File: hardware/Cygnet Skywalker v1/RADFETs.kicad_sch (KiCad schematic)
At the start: 14 parts, among them Q1 NJFET, Q2 NJFET, Q5 NJFET, Q6 NMOS, Q7 NMOS, Q8 NJFET, U10 INA260, U11 RM-VT01-A Readout Module, U12 VT01, U4 INA260, U6 VT01

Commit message: minor progress on pcb design
- more decoupling caps
- i2c address config
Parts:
- added C20, C21: 100n, symbol Device:C
- added C26: 10u, symbol Device:C
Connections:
- net +12V: now also C26.1
- net +3.3V: now also C20.1, C21.1
- net GND: now also C20.2, C21.2, C26.2

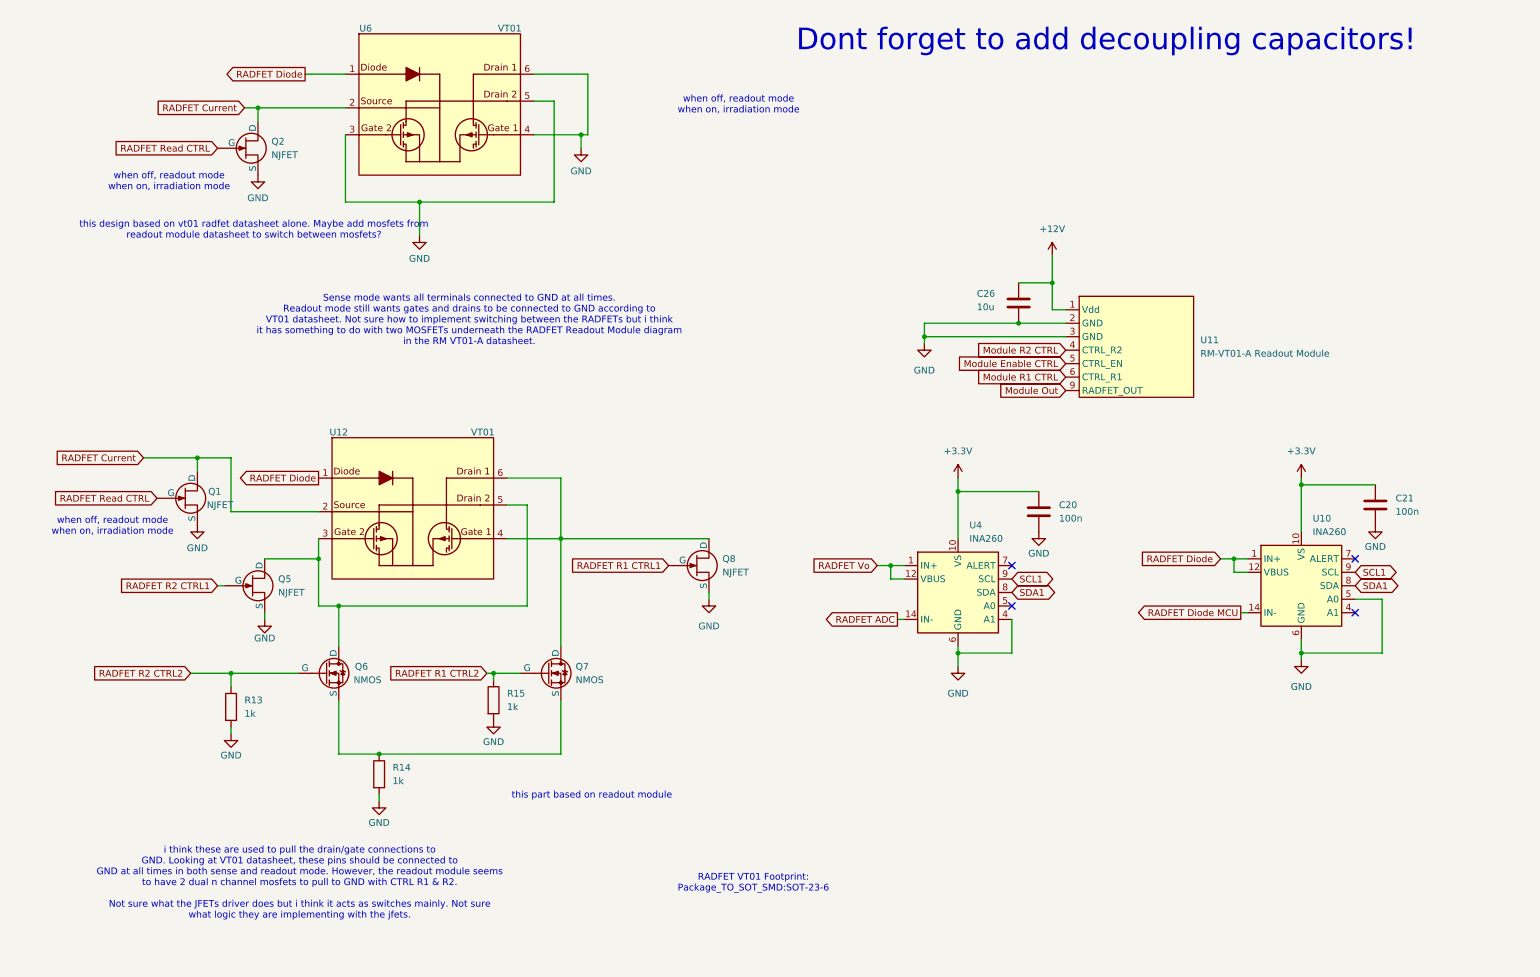
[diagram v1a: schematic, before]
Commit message: updated progress on PCB
-implemented 3.3v to 12v boost converter
-radfet readout circuitry done (i think)
-added readout circuitry from oresat & proves fc v5c board
-finished gps schematic (need footprint still)
-added few LEDs

main priorities:
-watchdog circuit
-calculate voltage div resistor values for 12v
-gps footprint
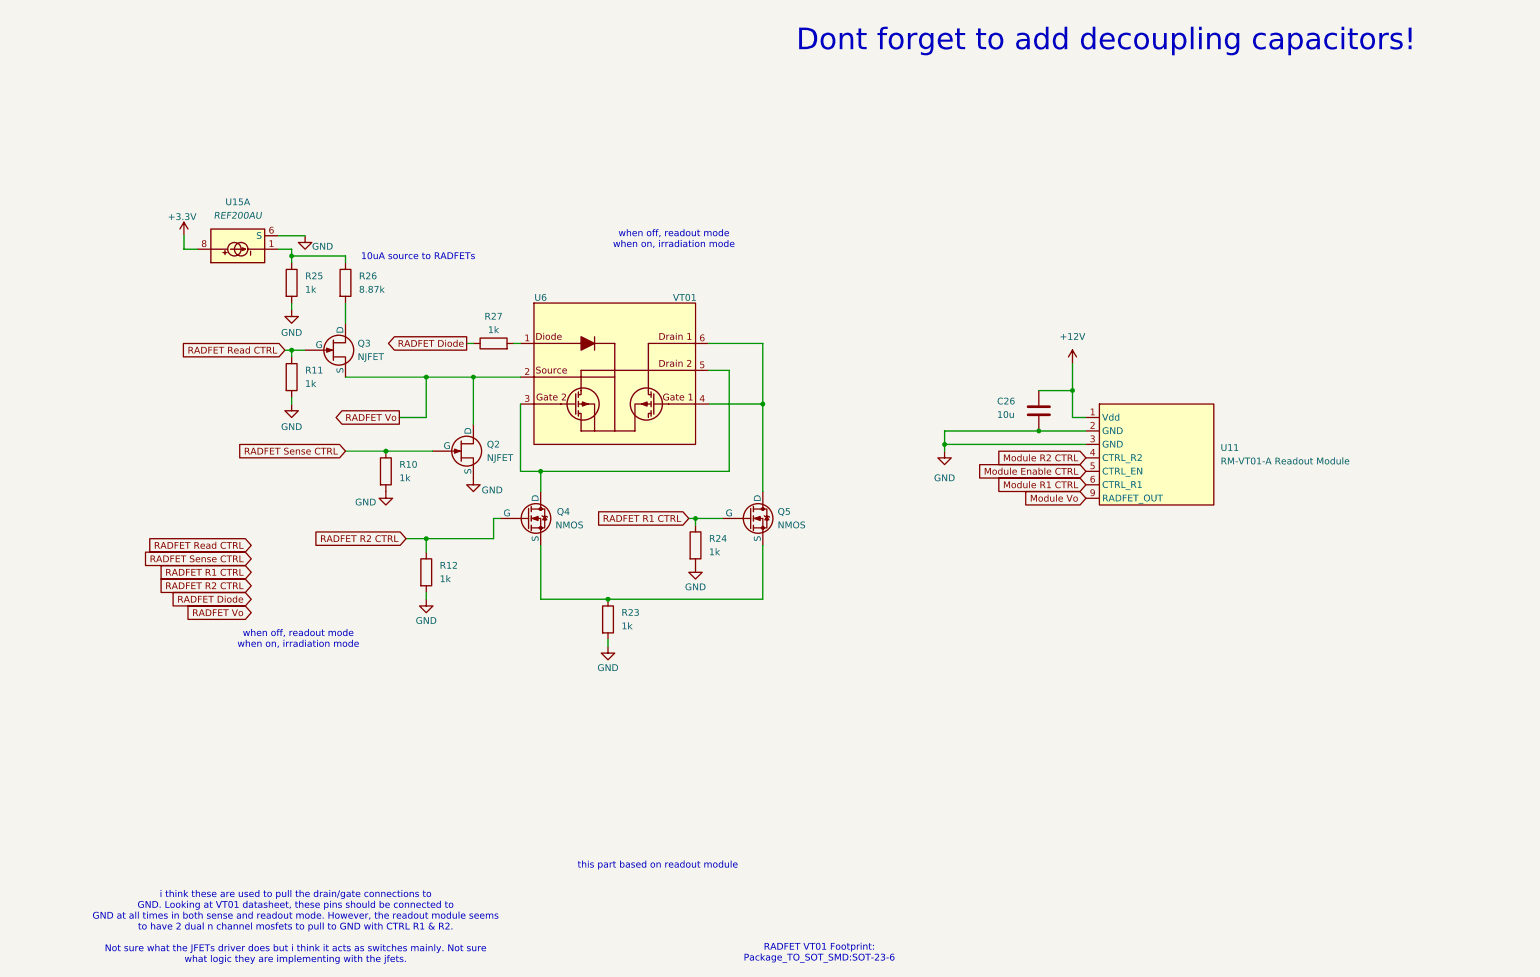
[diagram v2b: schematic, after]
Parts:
- removed C20, C21: 100n, symbol Device:C
- removed Q1, Q5, Q8: NJFET, symbol Simulation_SPICE:NJFET
- removed Q6, Q7: NMOS, symbol Simulation_SPICE:NMOS
- removed R13, R14, R15: 1k, symbol Device:R
- removed U10, U4: INA260, Package_SO:TSSOP-16_4.4x5mm_P0.65mm, symbol Sensor:INA260
- removed U12: VT01, Package_TO_SOT_SMD:SOT-23-6, symbol Varadis_RADFETs:VT01
- added Q3: NJFET, symbol Simulation_SPICE:NJFET
- added Q4, Q5: NMOS, symbol Simulation_SPICE:NMOS
- added R10, R11, R12, R23, R24, R25, R27: 1k, symbol Device:R
- added R26: 8.87k, symbol Device:R
- added U15: REF200AU, Package_SO:SOIC-8_3.9x4.9mm_P1.27mm, symbol Reference_Current:REF200AU
- U11: footprint (none) -> Skywalkerfeet:RM-VT01-A
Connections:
- net RADFET Current is gone; now on net RADFET Vo: Q2.1 (D), U6.2
- net +3.3V: now also U15.8
- net GND: now also R10.2, R11.2, R12.2, R23.2, R24.2, R25.2, U15.6 (S); no longer U6.3, U6.4, U6.5, U6.6
- net RADFET Diode: now also R27.1; no longer U6.1
- net RADFET Read CTRL: now also Q3.2 (G), R11.1; no longer Q2.2 (G)
- net RADFET Vo: now also Q3.3 (S)
- net Module Out renamed Module Vo
- new net: R27.2, U6.1
- new net: Q4.1 (D), U6.3, U6.5
- new net: Q5.1 (D), U6.4, U6.6
- new net: Q4.3 (S), Q5.3 (S), R23.1
- new net: Q3.1 (D), R26.2
- new net: R25.1, R26.1, U15.1
- new net RADFET R1 CTRL: Q5.2 (G), R24.1
- new net RADFET R2 CTRL: Q4.2 (G), R12.1
- new net RADFET Sense CTRL: Q2.2 (G), R10.1
- no-connect marks 4 -> 0
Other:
- note added: "10uA source to RADFETs"
- note removed: "Sense mode wants all terminals connected to GND at all times. Readout mode still wants gates and drains to be connected to GND according to VT01 datasheet. Not sure how to implement switching between the RADFETs but i think it has something to do with two MOSFETs underneath the RADFET Readout Module diagram in the RM VT01-A datasheet."
- note removed: "this design based on vt01 radfet datasheet alone. Maybe add mosfets from readout module datasheet to switch between mosfets?"
- moved on the sheet: C26, Q2, U11, U6

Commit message: carried over changes to schematic made on max's branch
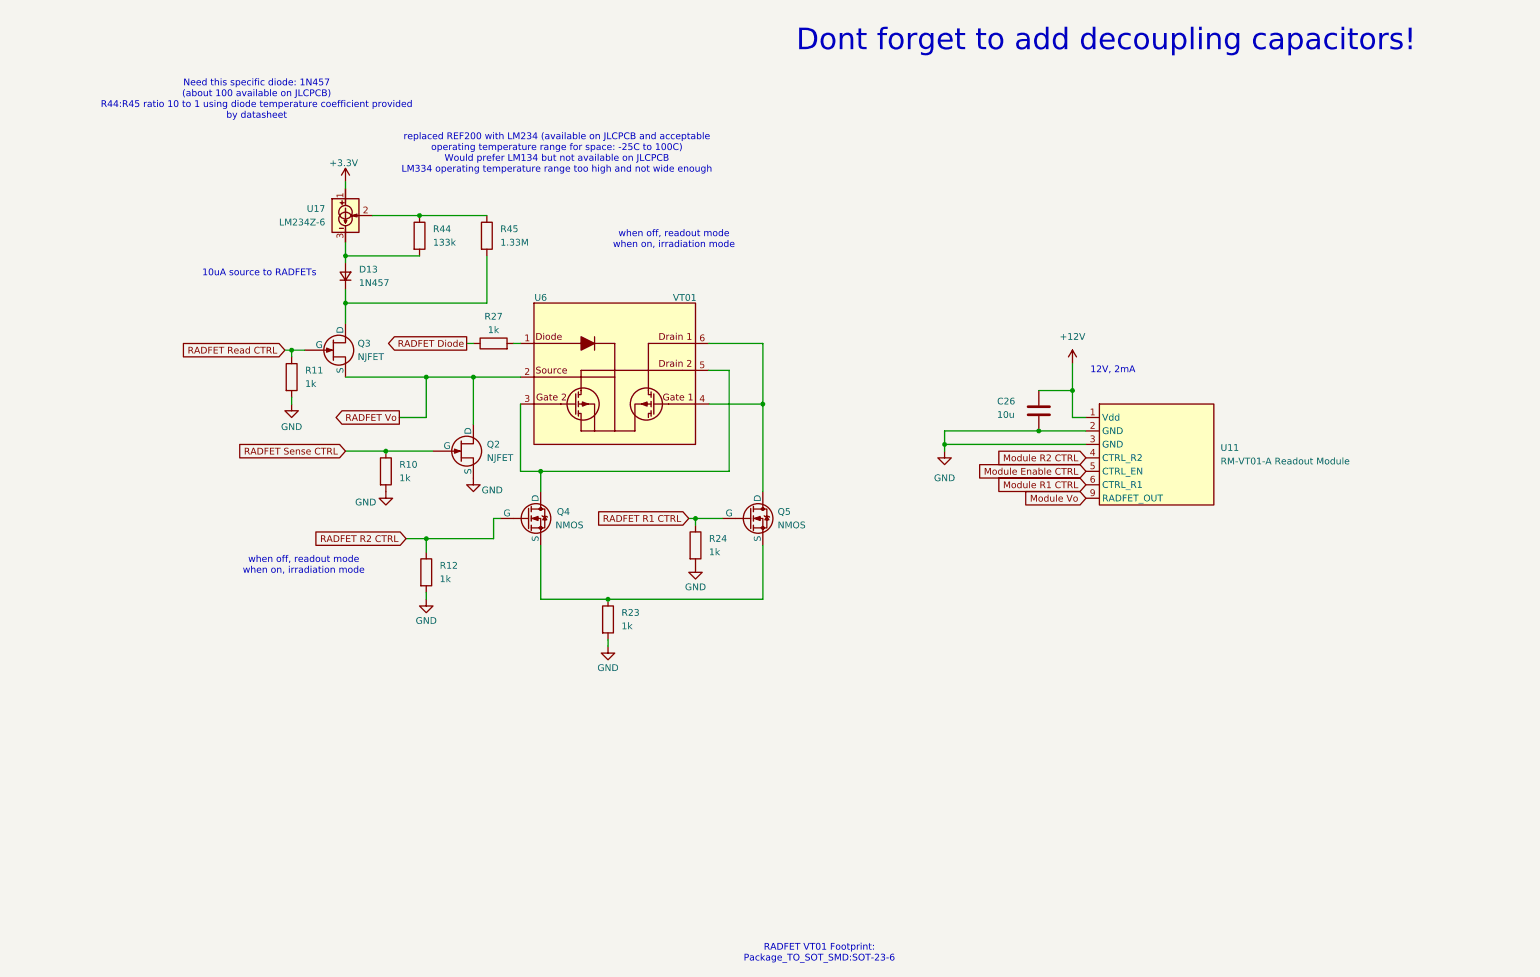
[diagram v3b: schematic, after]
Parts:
- removed R25: 1k, symbol Device:R
- removed R26: 8.87k, symbol Device:R
- removed U15: REF200AU, Package_SO:SOIC-8_3.9x4.9mm_P1.27mm, symbol Reference_Current:REF200AU
- added D13: 1N457, symbol Device:D_Small
- added R44: 133k, symbol Device:R
- added R45: 1.33M, symbol Device:R
- added U17: LM234Z-6, Package_TO_SOT_THT:TO-92_Inline, symbol Reference_Current:LM234Z-6
- C26: footprint (none) -> Capacitor_SMD:C_0402_1005Metric
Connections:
- net +3.3V: now also U17.1
- net at Q3.1 (D): now also D13.1 (K), R45.2
- new net: R44.1, R45.1, U17.2
- new net: D13.2 (A), R44.2, U17.3
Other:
- note added: "12V, 2mA"
- note added: "Need this specific diode: 1N457 (about 100 available on JLCPCB) R44:R45 ratio 10 to 1 using diode temperature coefficient provided by datasheet"
- note added: "replaced REF200 with LM234 (available on JLCPCB and acceptable operating temperature range for space: -25C to 100C) Would prefer LM134 but not available on JLCPCB LM334 operating temperature range too high and not wide enough"
- note removed: "i think these are used to pull the drain/gate connections to GND. Looking at VT01 datasheet, these pins should be connected to GND at all times in both sense and readout mode. However, the readout module seems to have 2 dual n channel mosfets to pull to GND with CTRL R1 & R2. Not sure what the JFETs driver does but i think it acts as switches mainly. Not sure what logic they are implementing with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"
- note removed: "this part based on readout module"

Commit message: brought over changes made on max branch
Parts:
- added C32: 10u, Capacitor_SMD:C_0402_1005Metric, symbol Device:C
- renumbered C26 to C33, D13 to D11, R44 to R21, R45 to R22, R27 to R23, R11 to R24, R10 to R25, R12 to R26, R24 to R27, R23 to R28
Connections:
- net +3.3V: now also C32.1
- net GND: now also C32.2
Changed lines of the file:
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@@
+	)
+	(junction
+		(at 68.58 41.91)
+		(diameter 0)
+		(color 0 0 0 0)
 	)
 	(junction
@@
 	(wire
 		(pts
+			(xy 68.58 41.91) (xy 68.58 49.53)
+		)
+		(stroke
+			(width 0)
+			(type default)
+		)
+	)
+	(wire
+		(pts
 			(xy 96.52 115.57) (xy 96.52 111.76)
 		)
@@
 	(wire
 		(pts
-			(xy 68.58 48.26) (xy 68.58 49.53)
+			(xy 68.58 40.64) (xy 68.58 41.91)
 		)
 		(stroke
@@
 		(pts
 			(xy 147.32 90.17) (xy 147.32 78.74)
+		)
+		(stroke
+			(width 0)
+			(type default)
+		)
+	)
+	(wire
+		(pts
+			(xy 57.15 41.91) (xy 68.58 41.91)
 		)
 		(stroke
@@
 		(dnp no)
 		(fields_autoplaced yes)
-		(property "Reference" "R23"
+		(property "Reference" "R28"
 			(at 120.65 129.5399 0)
 			(effects
@@
 			(project "Cygnet Skywalker v1"
 				(path "/f674abc6-f811-4b69-a04b-9059ca6b6a44/33e54b08-8438-48ba-af26-405155868428"
-					(reference "R23")
+					(reference "R28")
 					(unit 1)
 				)
@@
 		(dnp no)
 		(fields_autoplaced yes)
-		(property "Reference" "R12"
+		(property "Reference" "R26"
 			(at 86.36 120.6499 0)
 			(effects
@@
 			(project "Cygnet Skywalker v1"
 				(path "/f674abc6-f811-4b69-a04b-9059ca6b6a44/33e54b08-8438-48ba-af26-405155868428"
-					(reference "R12")
+					(reference "R26")
 					(unit 1)
 				)
@@
 		(on_board yes)
 		(dnp no)
-		(property "Reference" "C26"
+		(property "Reference" "C33"
 			(at 191.516 89.662 0)
 			(effects
@@
 			(project "Cygnet Skywalker v1"
 				(path "/f674abc6-f811-4b69-a04b-9059ca6b6a44/33e54b08-8438-48ba-af26-405155868428"
-					(reference "C26")
+					(reference "C33")
 					(unit 1)
 				)
@@
 		(dnp no)
 		(fields_autoplaced yes)
-		(property "Reference" "R11"
+		(property "Reference" "R24"
 			(at 60.96 83.8199 0)
 			(effects
@@
 			(project "Cygnet Skywalker v1"
 				(path "/f674abc6-f811-4b69-a04b-9059ca6b6a44/33e54b08-8438-48ba-af26-405155868428"
-					(reference "R11")
+					(reference "R24")
 					(unit 1)
 				)
@@
 		(on_board yes)
 		(dnp no)
-		(property "Reference" "R27"
+		(property "Reference" "R23"
 			(at 96.52 73.66 90)
 			(effects
@@
 			(project "Cygnet Skywalker v1"
 				(path "/f674abc6-f811-4b69-a04b-9059ca6b6a44/33e54b08-8438-48ba-af26-405155868428"
-					(reference "R27")
+					(reference "R23")
 					(unit 1)
 				)
@@
 	(symbol
 		(lib_id "power:+3.3V")
-		(at 68.58 48.26 0)
+		(at 68.58 40.64 0)
 		(unit 1)
 		(exclude_from_sim no)
@@
 		(dnp no)
 		(property "Reference" "#PWR0105"
-			(at 68.58 52.07 0)
+			(at 68.58 44.45 0)
 			(effects
 				(font
@@
 		)
 		(property "Value" "+3.3V"
-			(at 65.532 44.704 0)
+			(at 65.532 37.084 0)
 			(effects
 				(font
@@
 		)
 		(property "Footprint" ""
-			(at 68.58 48.26 0)
+			(at 68.58 40.64 0)
 			(effects
 				(font
@@
 		)
 		(property "Datasheet" ""
-			(at 68.58 48.26 0)
+			(at 68.58 40.64 0)
 			(effects
 				(font
@@
 		)
 		(property "Description" "Power symbol creates a global label with name \"+3.3V\""
-			(at 68.58 48.26 0)
+			(at 68.58 40.64 0)
 			(effects
 				(font
@@
 		(dnp no)
 		(fields_autoplaced yes)
-		(property "Reference" "R45"
+		(property "Reference" "R22"
 			(at 97.79 57.1499 0)
 			(effects
@@
 			(project "Cygnet Skywalker v1"
 				(path "/f674abc6-f811-4b69-a04b-9059ca6b6a44/33e54b08-8438-48ba-af26-405155868428"
-					(reference "R45")
+					(reference "R22")
 					(unit 1)
 				)
@@
 		(dnp no)
 		(fields_autoplaced yes)
-		(property "Reference" "D13"
+		(property "Reference" "D11"
 			(at 71.12 64.7699 90)
 			(effects
@@
 			(project ""
 				(path "/f674abc6-f811-4b69-a04b-9059ca6b6a44/33e54b08-8438-48ba-af26-405155868428"
-					(reference "D13")
+					(reference "D11")
 					(unit 1)
 				)
@@
 		(dnp no)
 		(fields_autoplaced yes)
-		(property "Reference" "R24"
+		(property "Reference" "R27"
 			(at 137.16 115.5699 0)
 			(effects
@@
 			(project "Cygnet Skywalker v1"
 				(path "/f674abc6-f811-4b69-a04b-9059ca6b6a44/33e54b08-8438-48ba-af26-405155868428"
-					(reference "R24")
+					(reference "R27")
 					(unit 1)
 				)
@@
 		(dnp no)
 		(fields_autoplaced yes)
-		(property "Reference" "R10"
+		(property "Reference" "R25"
 			(at 78.74 101.5999 0)
 			(effects
@@
 			(project "Cygnet Skywalker v1"
 				(path "/f674abc6-f811-4b69-a04b-9059ca6b6a44/33e54b08-8438-48ba-af26-405155868428"
-					(reference "R10")
+					(reference "R25")
 					(unit 1)
 				)
@@
 		(dnp no)
 		(fields_autoplaced yes)
-		(property "Reference" "R44"
+		(property "Reference" "R21"
 			(at 85.09 57.1499 0)
 			(effects
@@
 			(project "Cygnet Skywalker v1"
 				(path "/f674abc6-f811-4b69-a04b-9059ca6b6a44/33e54b08-8438-48ba-af26-405155868428"
-					(reference "R44")
+					(reference "R21")
 					(unit 1)
 				)
@@
 					(unit 1)
 				)
+			)
+		)
+	)
+	(symbol
+		(lib_id "power:GND")
+		(at 57.15 49.53 0)
+		(unit 1)
+		(exclude_from_sim no)
+		(in_bom yes)
+		(on_board yes)
+		(dnp no)
+		(property "Reference" "#PWR012"
+			(at 57.15 55.88 0)
+			(effects
+				(font
+					(size 1.27 1.27)
+				)
+				(hide yes)
+			)
+		)
+		(property "Value" "GND"
+			(at 53.34 51.562 0)
+			(effects
+				(font
+					(size 1.27 1.27)
+				)
+			)
+		)
+		(property "Footprint" ""
+			(at 57.15 49.53 0)
+			(effects
+				(font
+					(size 1.27 1.27)
+				)
+				(hide yes)
+			)
+		)
+		(property "Datasheet" ""
+			(at 57.15 49.53 0)
+			(effects
+				(font
+					(size 1.27 1.27)
+				)
+				(hide yes)
+			)
+		)
+		(property "Description" "Power symbol creates a global label with name \"GND\" , ground"
+			(at 57.15 49.53 0)
+			(effects
+				(font
+					(size 1.27 1.27)
+				)
+				(hide yes)
+			)
+		)
+		(pin "1"
+		)
+		(instances
+			(project "Cygnet Skywalker v1"
+				(path "/f674abc6-f811-4b69-a04b-9059ca6b6a44/33e54b08-8438-48ba-af26-405155868428"
+					(reference "#PWR012")
+					(unit 1)
+				)
+			)
+		)
+	)
+	(symbol
+		(lib_id "Device:C")
+		(at 57.15 45.72 0)
+		(unit 1)
+		(exclude_from_sim no)
+		(in_bom yes)
+		(on_board yes)
+		(dnp no)
+		(property "Reference" "C32"
+			(at 49.276 43.942 0)
+			(effects
+				(font
+					(size 1.27 1.27)
+				)
+				(justify left)
+			)
+		)
+		(property "Value" "10u"
+			(at 49.276 46.482 0)
+			(effects
+				(font
+					(size 1.27 1.27)
+				)
+				(justify left)
+			)
+		)
+		(property "Footprint" "Capacitor_SMD:C_0402_1005Metric"
+			(at 58.1152 49.53 0)
+			(effects
+				(font
+					(size 1.27 1.27)
+				)
+				(hide yes)
+			)
+		)
+		(property "Datasheet" "~"
+			(at 57.15 45.72 0)
+			(effects
+				(font
+					(size 1.27 1.27)
+				)
+				(hide yes)
+			)
+		)
+		(property "Description" ""
+			(at 57.15 45.72 0)
+			(effects
+				(font
+					(size 1.27 1.27)
+				)
+			)
+		)
+		(pin "1"
+		)
+		(pin "2"
+		)
+		(instances
+			(project "Cygnet Skywalker v1"
+				(path "/f674abc6-f811-4b69-a04b-9059ca6b6a44/33e54b08-8438-48ba-af26-405155868428"
+					(reference "C32")
+					(unit 1)
+				)
